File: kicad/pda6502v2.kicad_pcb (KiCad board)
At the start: 4 copper layers, 100 x 100 mm, 80 parts, among them J1 GPIO1, J2 GPIO2, J3 UART, J4 Screw_Terminal_01x02, J5 Conn_02x04_Odd_Even, J6 ICSP, SW1 SW_Push, U1 W65C02SxP, U10 LT3030, U11 SC28L92A1B, U2 W65C22SxP, U3 W65C22SxP, U4 DS1818, U5 AS6C4008-55PCN, U6 AS6C4008-55PCN, U7 AT25M01, U8 ICE40HX4K-TQ144, U9 TLV1117-33, X1 8 MHz, X2 3.6864 MHz

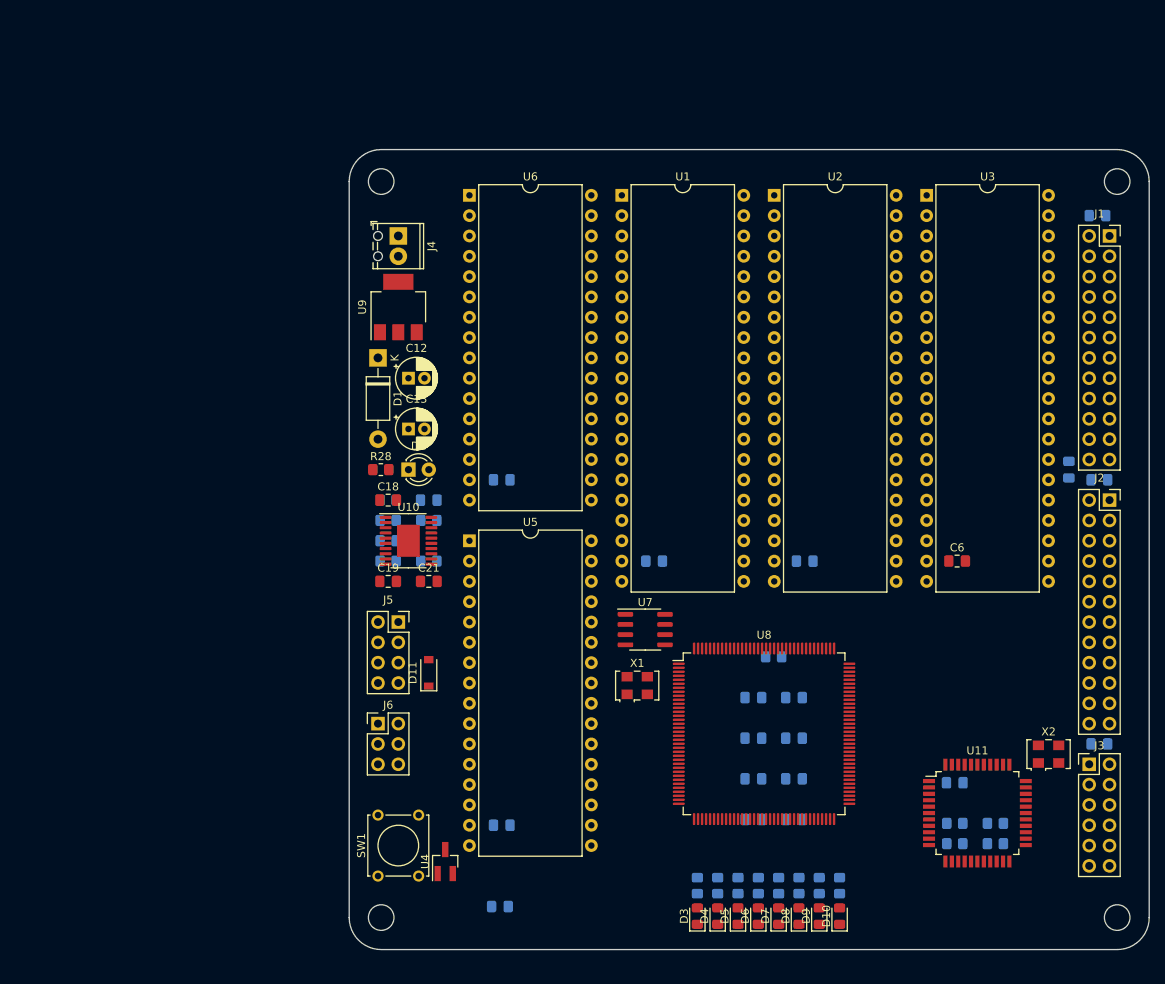
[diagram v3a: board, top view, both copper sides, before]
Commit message: Headers for SPI and EXT (FPGA expansion)
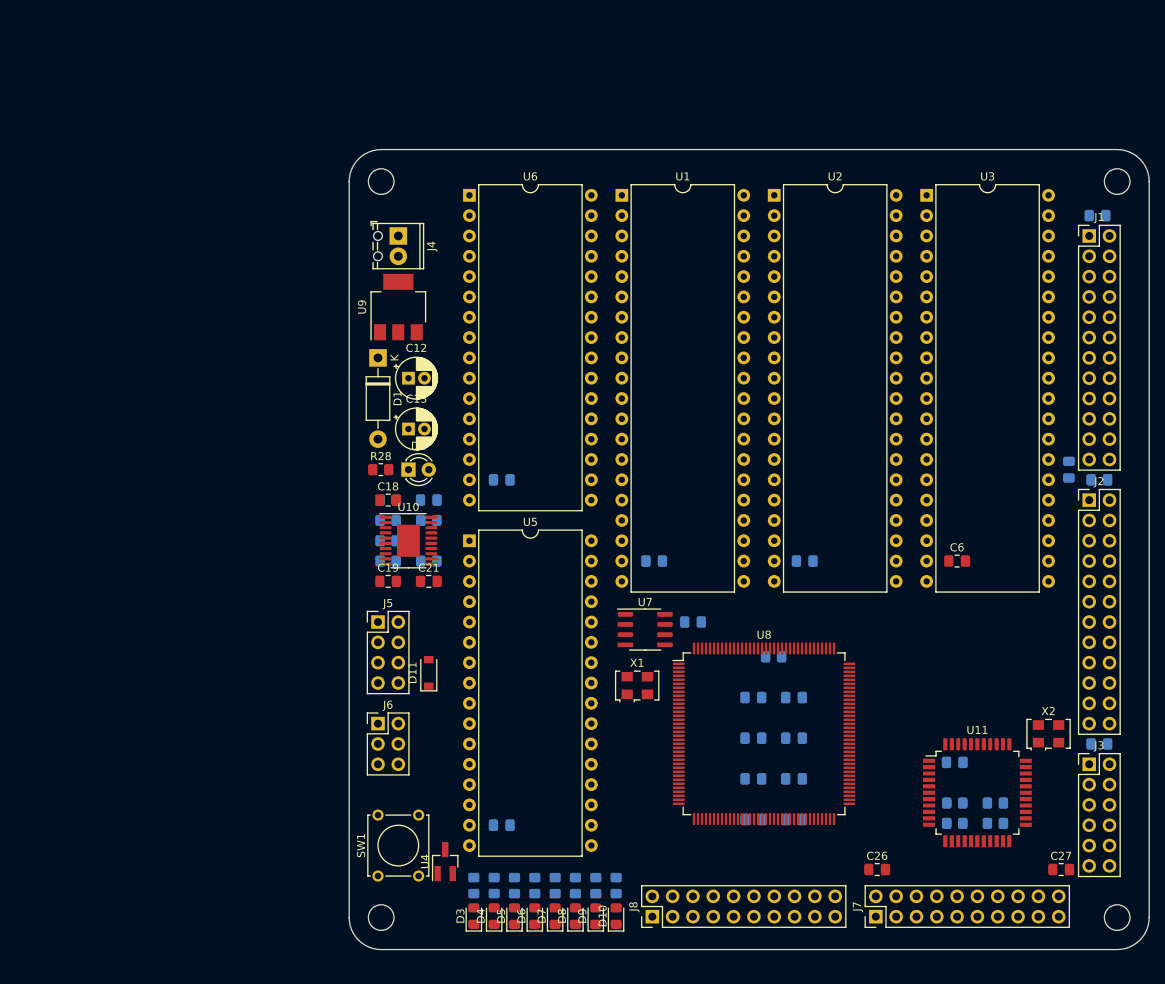
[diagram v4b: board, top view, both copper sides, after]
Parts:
- added C26: 0.1μF, Capacitor_SMD:C_0805_2012Metric_Pad1.18x1.45mm_HandSolder, F.Cu at (164.0, 130.0)
- added C27: 0.1μF, Capacitor_SMD:C_0805_2012Metric_Pad1.18x1.45mm_HandSolder, F.Cu at (187.0, 130.0)
- added J7: Conn_02x10_Odd_Even, Connector_PinHeader_2.54mm:PinHeader_2x10_P2.54mm_Vertical, F.Cu at (163.8, 135.9)
- added J8: Conn_02x10_Odd_Even, Connector_PinHeader_2.54mm:PinHeader_2x10_P2.54mm_Vertical, F.Cu at (135.9, 135.9)
- J1, J2: footprint Connector_PinSocket_2.54mm:PinSocket_2x12_P2.54mm_Vertical -> Connector_PinHeader_2.54mm:PinHeader_2x12_P2.54mm_Vertical
- J5: footprint Connector_PinSocket_2.54mm:PinSocket_2x04_P2.54mm_Vertical -> Connector_PinHeader_2.54mm:PinHeader_2x04_P2.54mm_Vertical
- moved C10 43.0 mm to (141.0, 99.1)
- moved D3 27.9 mm to (113.6, 135.8)
- moved D7 27.9 mm to (123.7, 135.8)
- moved R29 27.9 mm to (113.6, 132.0)
- moved R33 27.9 mm to (123.7, 132.0)
- moved D10 27.9 mm to (131.4, 135.8)
- moved D4 27.9 mm to (116.1, 135.8)
- moved D5 27.9 mm to (118.7, 135.8)
- moved D8 27.9 mm to (126.3, 135.8)
- moved D9 27.9 mm to (128.8, 135.8)
- moved R30 27.9 mm to (116.1, 132.0)
- moved R31 27.9 mm to (118.7, 132.0)
- moved R34 27.9 mm to (126.3, 132.0)
- moved R35 27.9 mm to (128.8, 132.0)
- moved R36 27.9 mm to (131.4, 132.0)
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
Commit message: ARMSID instead of second 512 KiB RAM
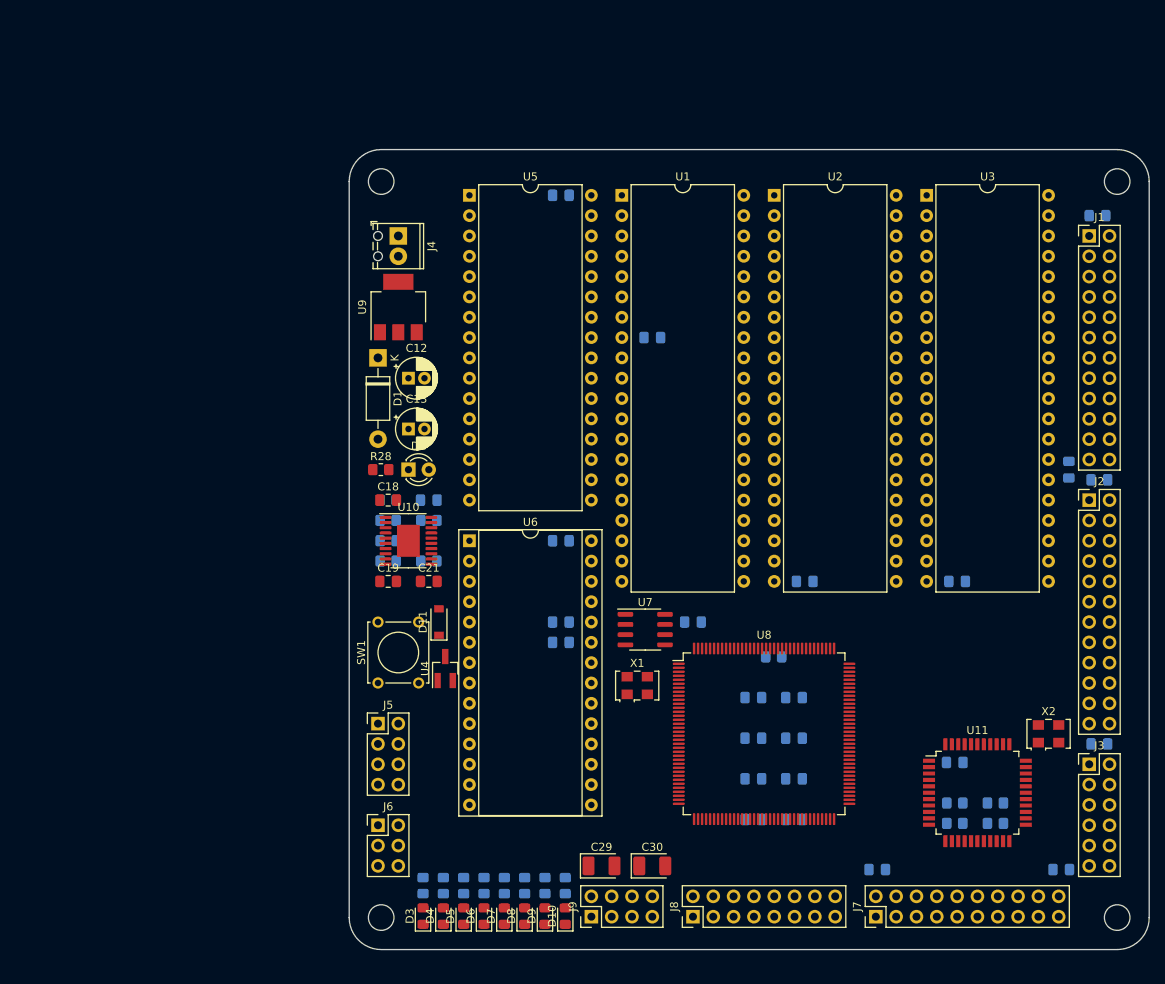
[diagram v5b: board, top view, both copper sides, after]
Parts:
- added C28: ?, Capacitor_SMD:C_0805_2012Metric_Pad1.18x1.45mm_HandSolder, B.Cu at (124.5, 99.1)
- added C29: 10uF, Capacitor_Tantalum_SMD:CP_EIA-3528-15_AVX-H_Pad1.50x2.35mm_HandSolder, F.Cu at (129.5, 129.5)
- added C30: 10uF, Capacitor_Tantalum_SMD:CP_EIA-3528-15_AVX-H_Pad1.50x2.35mm_HandSolder, F.Cu at (135.9, 129.5)
- added C31: ?, Capacitor_SMD:C_0805_2012Metric_Pad1.18x1.45mm_HandSolder, B.Cu at (124.5, 101.6)
- added J9: SID, Connector_PinHeader_2.54mm:PinHeader_2x04_P2.54mm_Vertical, F.Cu at (128.3, 135.9)
- C26, C27, C6: moved to B.Cu
- J7: value Conn_02x10_Odd_Even -> SPI
- J8: value Conn_02x10_Odd_Even -> FPGA_EXT; footprint Connector_PinHeader_2.54mm:PinHeader_2x10_P2.54mm_Vertical -> Connector_PinHeader_2.54mm:PinHeader_2x08_P2.54mm_Vertical
- U6: value AS6C4008-55PCN -> ARMSID; footprint Package_DIP:DIP-32_W15.24mm -> Package_DIP:DIP-28_W15.24mm_Socket
- moved C4 79.1 mm to (124.5, 45.7), turned to 180 degrees
- moved U5 43.2 mm to (113.0, 45.7)
- moved U6 43.2 mm to (113.0, 88.9)
- moved C1 27.9 mm to (135.9, 63.5)
- moved SW1 24.1 mm to (101.6, 106.7)
- moved U4 24.1 mm to (110.0, 104.9)
- moved J5 12.7 mm to (101.6, 111.8)
- moved J6 12.7 mm to (101.6, 124.5)
- moved C9 10.6 mm to (124.5, 88.9), turned to 180 degrees
- moved D11 6.48 mm to (109.2, 99.1)
- moved D10 6.35 mm to (125.0, 135.8)
- moved D4 6.35 mm to (109.8, 135.8)
- moved D6 6.35 mm to (114.8, 135.8)
- moved R30 6.35 mm to (109.8, 132.0)
- moved R32 6.35 mm to (114.8, 132.0)
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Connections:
- C9 pad 1: +3V3 -> +5V
- J8 pad 10: /EXT_14 -> /EXT_12
- J8 pad 12: /EXT_15 -> /EXT_13
- J8 pad 14: /EXT_16 -> /EXT_14
- J8 pad 16: /EXT_17 -> /EXT_15
- J8 pad 2: /EXT_10 -> /EXT_8
- J8 pad 4: /EXT_11 -> /EXT_9
- J8 pad 6: /EXT_12 -> /EXT_10
- J8 pad 8: /EXT_13 -> /EXT_11
- U5 pad 22: /RAM_HI_~CS -> /RAM_~CS
- U5 pad 24: /RAM_HI_~CS -> /RAM_~CS
- U6 pad 1: /A18 -> (no net)
- U6 pad 10: /A2 -> /A1
- U6 pad 11: /A1 -> /A2
- U6 pad 12: /A0 -> /A3
- U6 pad 13: /D0 -> /A4
- U6 pad 14: /D1 -> GND
- U6 pad 15: /D2 -> /D0
- U6 pad 16: GND -> /D1
- U6 pad 17: /D3 -> /D2
- U6 pad 18: /D4 -> /D3
- U6 pad 19: /D5 -> /D4
- U6 pad 2: /A16 -> (no net)
- U6 pad 20: /D6 -> /D5
- U6 pad 21: /D7 -> /D6
- U6 pad 22: /RAM_LO_~CS -> /D7
- U6 pad 23: /A10 -> /SID_Y
- U6 pad 24: /RAM_LO_~CS -> /SID_X
- U6 pad 25: /A11 -> +5V
- U6 pad 26: /A9 -> Net-(C30-Pad1)
- U6 pad 27: /A8 -> Net-(C29-Pad1)
- U6 pad 28: /A13 -> +5V
- U6 pad 3: /A14 -> (no net)
- U6 pad 4: /A12 -> (no net)
- U6 pad 5: /A7 -> /~RESET
- U6 pad 6: /A6 -> /CLOCK
- U6 pad 7: /A5 -> /R~W
- U6 pad 8: /A4 -> /SID_~CS
- U6 pad 9: /A3 -> /A0
- U8 pad 61: /RAM_LO_~CS -> /RAM_~CS
- U8 pad 62: /RAM_HI_~CS -> /SID_~CS

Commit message: Rearranged FPGA pin allocations for easier routing
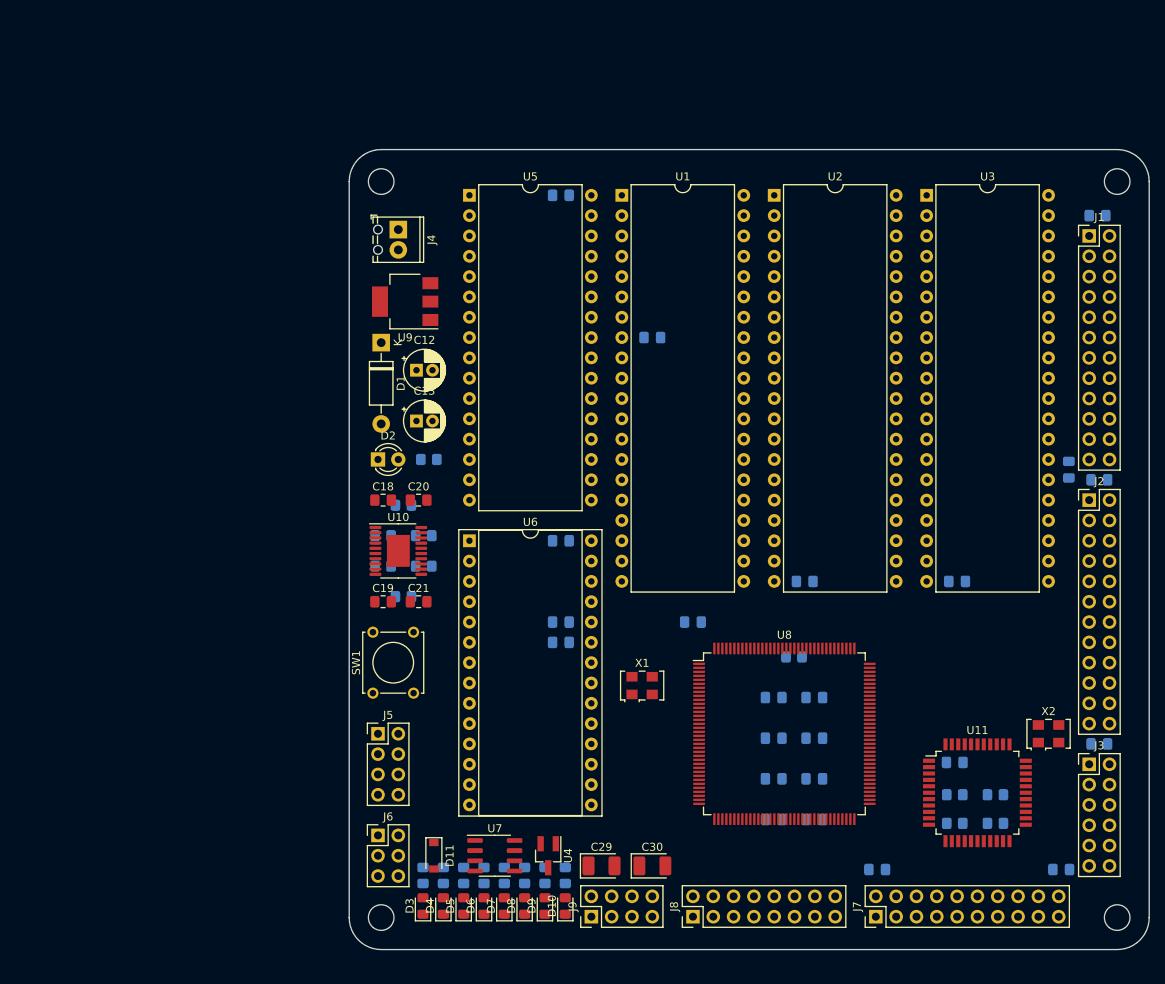
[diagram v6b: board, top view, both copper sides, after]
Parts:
- C20: moved to F.Cu
- R28: moved to B.Cu
- moved U7 33.9 mm to (116.2, 128.3)
- moved D11 29.2 mm to (108.6, 128.3), turned to 270 degrees
- moved U4 26.7 mm to (122.9, 128.3), turned to 270 degrees
- moved R28 6.13 mm to (108.0, 78.7)
- moved R27 4.84 mm to (104.8, 95.9)
- moved D2 4.02 mm to (101.6, 78.7)
- moved R26 3.24 mm to (102.2, 92.1)
- moved C21 2.84 mm to (106.7, 96.5)
- moved C19 2.62 mm to (102.2, 96.5)
- moved C11 2.54 mm to (151.1, 123.7)
- moved C14 2.54 mm to (151.1, 118.7)
- moved C15 2.54 mm to (151.1, 113.6)
- moved C16 2.54 mm to (151.1, 108.5)
- moved C17 2.54 mm to (156.1, 123.7)
- moved C22 2.54 mm to (156.1, 118.7)
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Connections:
- J8 pad 10: /EXT_12 -> /EXT_9
- J8 pad 11: /EXT_5 -> /EXT_10
- J8 pad 12: /EXT_13 -> /EXT_11
- J8 pad 13: /EXT_6 -> /EXT_12
- J8 pad 14: /EXT_14 -> /EXT_13
- J8 pad 15: /EXT_7 -> /EXT_14
- J8 pad 2: /EXT_8 -> /EXT_1
- J8 pad 3: /EXT_1 -> /EXT_2
- J8 pad 4: /EXT_9 -> /EXT_3
- J8 pad 5: /EXT_2 -> /EXT_4
- J8 pad 6: /EXT_10 -> /EXT_5
- J8 pad 7: /EXT_3 -> /EXT_6
- J8 pad 8: /EXT_11 -> /EXT_7
- J8 pad 9: /EXT_4 -> /EXT_8
- U8 pad 1: Net-(U8-Pad1) -> /R~W
- U8 pad 10: Net-(U8-Pad10) -> /~NMIRQ
- U8 pad 101: /UART_~WRN -> Net-(U8-Pad101)
- U8 pad 102: /UART_~RDN -> Net-(U8-Pad102)
- U8 pad 104: /UART_RXA~IRQ -> /VIA2_~IRQ
- U8 pad 105: /UART_RXB~IRQ -> /VIA2_~CS
- U8 pad 106: /UART_TXA~IRQ -> /VIA1_~IRQ
- U8 pad 107: /UART_TXB~IRQ -> /VIA1_~CS
- U8 pad 11: Net-(U8-Pad11) -> /SYNC
- U8 pad 110: Net-(U8-Pad110) -> /A0
- U8 pad 112: Net-(U8-Pad112) -> /A1
- U8 pad 113: Net-(U8-Pad113) -> /A2
- U8 pad 114: Net-(U8-Pad114) -> /A3
- U8 pad 115: Net-(U8-Pad115) -> /A4
- U8 pad 116: /~VECPULL -> /A5
- U8 pad 117: /READY -> /A6
- U8 pad 118: /~IRQ -> /A7
- U8 pad 119: /~MLOCK -> /A8
- U8 pad 120: /~NMIRQ -> /A9
- U8 pad 121: /SYNC -> /A10
- U8 pad 122: /R~W -> /A11
- U8 pad 124: /BUSEN -> /A12
- U8 pad 125: /CLOCK -> /A13
- U8 pad 128: /CLOCKSRC -> /A14
- U8 pad 129: /~SETOV -> /A15
- U8 pad 130: /RESET -> /A16
- U8 pad 134: /~RESET -> /A17
- U8 pad 135: Net-(U8-Pad135) -> /A18
- U8 pad 136: Net-(U8-Pad136) -> /D0
- U8 pad 137: Net-(U8-Pad137) -> /D1
- U8 pad 138: Net-(U8-Pad138) -> /D2
- U8 pad 139: Net-(U8-Pad139) -> /D3
- U8 pad 141: Net-(U8-Pad141) -> /D4
- U8 pad 142: Net-(U8-Pad142) -> /D5
- U8 pad 143: Net-(U8-Pad143) -> /D6
- U8 pad 144: Net-(U8-Pad144) -> /D7
- U8 pad 15: Net-(U8-Pad15) -> /RAM_~CS
- U8 pad 19: Net-(U8-Pad19) -> /CLOCK
- U8 pad 2: Net-(U8-Pad2) -> /BUSEN
- U8 pad 20: Net-(U8-Pad20) -> /CLOCKSRC
- U8 pad 22: Net-(U8-Pad22) -> /RESET
- U8 pad 23: Net-(U8-Pad23) -> /~RESET
- U8 pad 24: Net-(U8-Pad24) -> /SID_~CS
- U8 pad 3: Net-(U8-Pad3) -> /~SETOV
- U8 pad 37: /D0 -> Net-(U8-Pad37)
- U8 pad 38: /D1 -> /EXT_0
- U8 pad 39: /D2 -> /EXT_1
- U8 pad 4: Net-(U8-Pad4) -> /~VECPULL
- U8 pad 41: /D3 -> /EXT_2
- U8 pad 42: /D4 -> /EXT_3
- U8 pad 43: /D5 -> /EXT_4
- U8 pad 44: /D6 -> /EXT_5
- U8 pad 45: /D7 -> /EXT_6
- U8 pad 47: Net-(U8-Pad47) -> /EXT_7
- U8 pad 48: Net-(U8-Pad48) -> /EXT_8
- U8 pad 49: Net-(U8-Pad49) -> /EXT_9
- U8 pad 52: /VIA1_~IRQ -> /EXT_10
- U8 pad 55: /VIA1_~CS -> /EXT_11
- U8 pad 56: /VIA2_~IRQ -> /EXT_12
- U8 pad 60: /VIA2_~CS -> /EXT_13
- U8 pad 61: /RAM_~CS -> /EXT_14
- U8 pad 62: /SID_~CS -> /EXT_15
- U8 pad 7: Net-(U8-Pad7) -> /READY
- U8 pad 73: /A0 -> /SPI_MISO
- U8 pad 74: /A1 -> /SPI_MOSI
- U8 pad 75: /A2 -> /SPI_CLOCK
- U8 pad 76: /A3 -> /SPI_CS0
- U8 pad 78: /A4 -> /SPI_CS1
- U8 pad 79: /A5 -> /SPI_CS2
- U8 pad 8: Net-(U8-Pad8) -> /~IRQ
- U8 pad 80: /A6 -> /SPI_CS3
- U8 pad 81: /A7 -> /SPI_CS4
- U8 pad 82: /A8 -> /SPI_CS5
- U8 pad 83: /A9 -> /SPI_CS6
- U8 pad 84: /A10 -> /SPI_CS7
- U8 pad 85: /A11 -> /SPI_EXP0
- U8 pad 87: /A12 -> /SPI_EXP1
- U8 pad 88: /A13 -> Net-(U8-Pad88)
- U8 pad 9: Net-(U8-Pad9) -> /~MLOCK
- U8 pad 90: /A14 -> /UART_~IRQ
- U8 pad 91: /A15 -> /UART_IM
- U8 pad 93: /A16 -> /UART_TXB~IRQ
- U8 pad 94: /A17 -> /UART_RXB~IRQ
- U8 pad 95: /A18 -> /UART_~RDN
- U8 pad 96: Net-(U8-Pad96) -> /UART_~WRN
- U8 pad 98: /UART_~IRQ -> /UART_TXA~IRQ
- U8 pad 99: /UART_IM -> /UART_RXA~IRQ
